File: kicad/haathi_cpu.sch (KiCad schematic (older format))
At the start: 116 parts

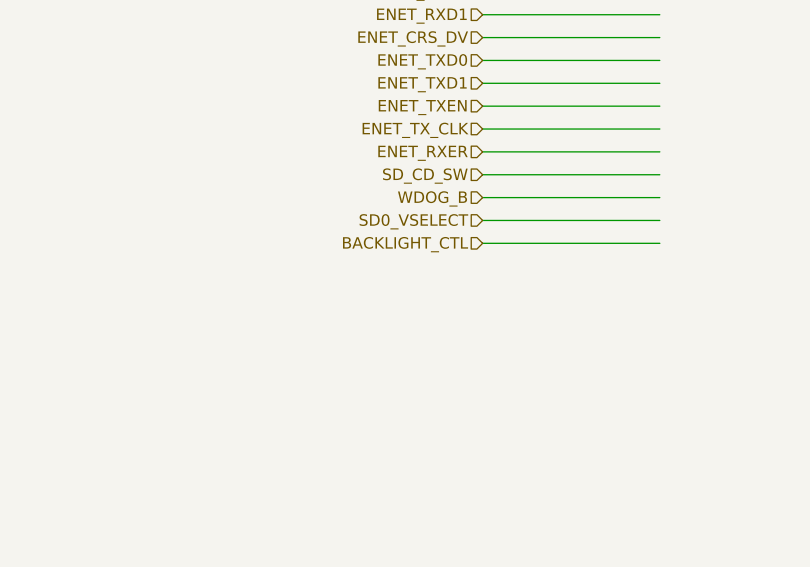
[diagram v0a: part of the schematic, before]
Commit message: Rearrange buttons and LED pin connections
LED pins go to PWM pins
Switches go to previously SPDIF_IN and OUT pins
FlexSPI 2 pins freed up

Signed-off-by: Kumar Abhishek <abhishek@theembeddedkitchen.net>
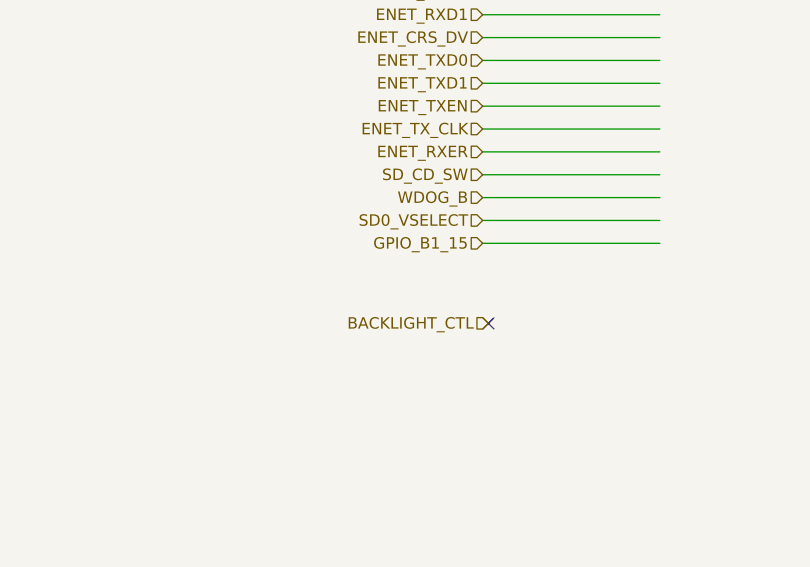
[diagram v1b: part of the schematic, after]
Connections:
- net labels added: GPIO_B1_15
- no-connect marks 2 -> 3
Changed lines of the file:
@@
 EESchema Schematic File Version 4
-LIBS:haathi_schematic-cache
+LIBS:haathi-cache
 EELAYER 26 0
 EELAYER END
 $Descr A2 23386 16535
 encoding utf-8
-Sheet 3 9
+Sheet 5 11
 Title "haathi_cam"
 Date "2018-03-11"
@@
 Text Label 3725 9000 0    50   ~ 0
 USB_OTG2_D-
-Text HLabel 10325 11050 0    50   Input ~ 0
+Text HLabel 10350 11400 0    50   Input ~ 0
 BACKLIGHT_CTL
 Wire Wire Line
@@
 Wire Wire Line
 	4100 9500 4250 9500
+Text Label 4250 9400 0    50   ~ 0
+GPIO_AD_B0_01
+Text Label 4250 9500 0    50   ~ 0
+GPIO_AD_B0_00
+Text HLabel 10325 11050 0    50   Input ~ 0
+GPIO_B1_15
+NoConn ~ 10350 11400
 Wire Bus Line
 	21850 4000 21850 4750
@@
 Wire Bus Line
 	9425 8000 9425 9800
-Text Label 4250 9400 0    50   ~ 0
-GPIO_AD_B0_01
-Text Label 4250 9500 0    50   ~ 0
-GPIO_AD_B0_00
 $EndSCHEMATC

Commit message: JTAG_MOD pullup and DNP pull down
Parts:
- added R?: 10k, symbol haathi_mayank:R
- R?: value 10k -> 10k_DNP
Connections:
- wire segments 567 -> 570
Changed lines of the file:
@@
 EESchema Schematic File Version 4
-LIBS:haathi-cache
+LIBS:haathi_cpu-cache
 EELAYER 26 0
 EELAYER END
 $Descr A2 23386 16535
 encoding utf-8
-Sheet 5 11
+Sheet 1 1
 Title "haathi_cam"
 Date "2018-03-11"
@@
 P 11850 2125
 F 0 "R?" V 11750 2075 50  0000 C CNN
-F 1 "10k" V 11966 2125 50  0000 C CNN
+F 1 "10k_DNP" V 11966 2125 50  0000 C CNN
 F 2 "" V 11780 2125 30  0000 C CNN
 F 3 "" H 11850 2125 30  0000 C CNN
@@
 GPIO_B1_15
 NoConn ~ 10350 11400
+$Comp
+L haathi_mayank:R R?
+U 1 1 5ADF8395
+P 11850 1650
+F 0 "R?" V 11750 1600 50  0000 C CNN
+F 1 "10k" V 11966 1650 50  0000 C CNN
+F 2 "" V 11780 1650 30  0000 C CNN
+F 3 "" H 11850 1650 30  0000 C CNN
+	1    11850 1650
+	1    0    0    -1
+$EndComp
+Wire Wire Line
+	11850 1800 11850 1950
+Text HLabel 11900 1300 2    50   Input ~ 0
+NVCC_GPIO_3V3
+Wire Wire Line
+	11850 1500 11850 1300
+Wire Wire Line
+	11850 1300 11900 1300
 Wire Bus Line
 	21850 4000 21850 4750

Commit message: Annotated schematic
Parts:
- gave numbers to parts that had none: 109

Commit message: ERC pass 1: Check and resolve the errors
Signed-off-by: Kumar Abhishek <abhishek@theembeddedkitchen.net>
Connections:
- net labels removed: VCC
- wire segments 570 -> 572
- no-connect marks 3 -> 5
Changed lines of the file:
@@
 EESchema Schematic File Version 4
-LIBS:haathi_schematic-cache
+LIBS:haathi-cache
 EELAYER 26 0
 EELAYER END
 $Descr A2 23386 16535
 encoding utf-8
-Sheet 3 9
+Sheet 5 11
 Title "haathi_cam"
 Date "2018-03-11"
@@
 U 1 1 5A82F303
 P 7300 3500
-F 0 "TP6" H 7453 3602 50  0000 L CNN
-F 1 "Test_Point_Probe" H 7453 3511 50  0000 L CNN
+F 0 "TP6" H 7525 3625 50  0000 C CNN
+F 1 "Test_Point_Probe" H 7775 3550 50  0000 C CNN
 F 2 "" H 7500 3500 50  0001 C CNN
 F 3 "~" H 7500 3500 50  0001 C CNN
@@
 	7050 2850 7200 2850
 Wire Wire Line
-	7200 2850 7200 4450
+	7200 2850 7200 4225
 Wire Wire Line
 	7200 4450 7200 4500
@@
 Wire Wire Line
 	7200 4800 7200 4850
-$Comp
-L power:VCC #PWR057
-U 1 1 5A8739EE
-P 7600 4450
-F 0 "#PWR057" H 7600 4300 50  0001 C CNN
-F 1 "VCC" H 7617 4623 50  0000 C CNN
-F 2 "" H 7600 4450 50  0001 C CNN
-F 3 "" H 7600 4450 50  0001 C CNN
-	1    7600 4450
-	1    0    0    -1
-$EndComp
-$Comp
-L power:PWR_FLAG #FLG010
-U 1 1 5A873B22
-P 7750 4500
-F 0 "#FLG010" H 7750 4575 50  0001 C CNN
-F 1 "PWR_FLAG" H 7750 4673 50  0000 C CNN
-F 2 "" H 7750 4500 50  0001 C CNN
-F 3 "" H 7750 4500 50  0001 C CNN
-	1    7750 4500
-	-1   0    0    1
-$EndComp
 Wire Wire Line
 	7500 4450 7600 4450
 Wire Wire Line
-	7750 4450 7750 4500
-Connection ~ 7600 4450
-Wire Wire Line
-	7600 4450 7750 4450
-Wire Wire Line
 	7050 2750 7150 2750
 Wire Wire Line
@@
 	6950 1350 6950 1650
 Wire Wire Line
-	6950 1650 7250 1650
+	6950 1650 7150 1650
 Connection ~ 6350 1350
 Wire Wire Line
@@
 	1    0    0    -1
 $EndComp
-$Comp
-L power:PWR_FLAG #FLG07
-U 1 1 5A953F34
-P 3350 4900
-F 0 "#FLG07" H 3350 4975 50  0001 C CNN
-F 1 "PWR_FLAG" H 3350 5073 50  0000 C CNN
-F 2 "" H 3350 4900 50  0001 C CNN
-F 3 "" H 3350 4900 50  0001 C CNN
-	1    3350 4900
-	-1   0    0    1
-$EndComp
 Wire Wire Line
 	6050 1350 6050 1150
@@
 	1    0    0    -1
 $EndComp
-$Comp
-L power:PWR_FLAG #FLG08
-U 1 1 5A98E537
-P 3350 5550
-F 0 "#FLG08" H 3350 5625 50  0001 C CNN
-F 1 "PWR_FLAG" H 3350 5723 50  0000 C CNN
-F 2 "" H 3350 5550 50  0001 C CNN
-F 3 "" H 3350 5550 50  0001 C CNN
-	1    3350 5550
-	-1   0    0    1
-$EndComp
 Wire Wire Line
 	1500 4900 1900 4900
@@
 	6150 11300 6250 11300
 Connection ~ 6250 11300
-Wire Wire Line
-	6250 11300 6450 11300
-$Comp
-L power:PWR_FLAG #FLG09
-U 1 1 5AEDE637
-P 6450 11300
-F 0 "#FLG09" H 6450 11375 50  0001 C CNN
-F 1 "PWR_FLAG" H 6200 11400 50  0000 C CNN
-F 2 "" H 6450 11300 50  0001 C CNN
-F 3 "" H 6450 11300 50  0001 C CNN
-	1    6450 11300
-	-1   0    0    1
-$EndComp
-Connection ~ 6450 11300
 $Comp
 L haathi_mayank:R R43
@@
 	1    0    0    -1
 $EndComp
-Connection ~ 3250 4900
-Wire Wire Line
-	3250 4900 3350 4900
 $Comp
 L power:+3V3 #PWR044
@@
 	1    0    0    -1
 $EndComp
-Connection ~ 3250 5550
-Wire Wire Line
-	3250 5550 3350 5550
 $Comp
 L power:+3V3 #PWR054
@@
 	2750 5550 3250 5550
 Wire Wire Line
-	6450 11300 6650 11300
-Wire Wire Line
 	9350 6300 9850 6300
 Text Label 9425 6300 0    50   ~ 0
@@
 	1    0    0    -1
 $EndComp
-Wire Wire Line
-	11850 1800 11850 1950
 Text HLabel 11900 1300 2    50   Input ~ 0
 NVCC_GPIO_3V3
@@
 Wire Wire Line
 	11850 1300 11900 1300
+Wire Wire Line
+	11850 1800 11850 1975
+Wire Wire Line
+	6250 11300 6650 11300
+$Comp
+L power:PWR_FLAG #FLG0103
+U 1 1 5B27BF1E
+P 7150 1525
+F 0 "#FLG0103" H 7150 1600 50  0001 C CNN
+F 1 "PWR_FLAG" H 7150 1699 50  0000 C CNN
+F 2 "" H 7150 1525 50  0001 C CNN
+F 3 "~" H 7150 1525 50  0001 C CNN
+	1    7150 1525
+	1    0    0    -1
+$EndComp
+Wire Wire Line
+	7150 1525 7150 1650
+Connection ~ 7150 1650
+Wire Wire Line
+	7150 1650 7250 1650
+$Comp
+L power:+3V3 #PWR0106
+U 1 1 5B337654
+P 7600 4450
+F 0 "#PWR0106" H 7600 4300 50  0001 C CNN
+F 1 "+3V3" H 7615 4623 50  0000 C CNN
+F 2 "" H 7600 4450 50  0001 C CNN
+F 3 "" H 7600 4450 50  0001 C CNN
+	1    7600 4450
+	1    0    0    -1
+$EndComp
+$Comp
+L power:PWR_FLAG #FLG0113
+U 1 1 5B33D17D
+P 7200 5550
+F 0 "#FLG0113" H 7200 5625 50  0001 C CNN
+F 1 "PWR_FLAG" H 7200 5724 50  0000 C CNN
+F 2 "" H 7200 5550 50  0001 C CNN
+F 3 "~" H 7200 5550 50  0001 C CNN
+	1    7200 5550
+	1    0    0    -1
+$EndComp
+$Comp
+L power:PWR_FLAG #FLG0114
+U 1 1 5B33E94E
+P 7100 4225
+F 0 "#FLG0114" H 7100 4300 50  0001 C CNN
+F 1 "PWR_FLAG" H 7450 4300 50  0000 C CNN
+F 2 "" H 7100 4225 50  0001 C CNN
+F 3 "~" H 7100 4225 50  0001 C CNN
+	1    7100 4225
+	1    0    0    -1
+$EndComp
+Wire Wire Line
+	7100 4225 7200 4225
+Connection ~ 7200 4225
+Wire Wire Line
+	7200 4225 7200 4450
+$Comp
+L power:PWR_FLAG #FLG0115
+U 1 1 5B3AC8F9
+P 8650 3050
+F 0 "#FLG0115" H 8650 3125 50  0001 C CNN
+F 1 "PWR_FLAG" H 8900 3125 50  0000 C CNN
+F 2 "" H 8650 3050 50  0001 C CNN
+F 3 "~" H 8650 3050 50  0001 C CNN
+	1    8650 3050
+	1    0    0    -1
+$EndComp
+NoConn ~ 7050 3850
+NoConn ~ 7050 3950
+$Comp
+L power:PWR_FLAG #FLG0116
+U 1 1 5B73D343
+P 8225 3450
+F 0 "#FLG0116" H 8225 3525 50  0001 C CNN
+F 1 "PWR_FLAG" H 8225 3624 50  0000 C CNN
+F 2 "" H 8225 3450 50  0001 C CNN
+F 3 "~" H 8225 3450 50  0001 C CNN
+	1    8225 3450
+	1    0    0    -1
+$EndComp
+Wire Wire Line
+	8225 3450 8225 3525
+Wire Wire Line
+	8225 3525 7300 3525
+Wire Wire Line
+	7300 3525 7300 3500
 Wire Bus Line
 	21850 4000 21850 4750
@@
 Wire Bus Line
 	9425 8000 9425 9800
+Connection ~ 7300 3500
 $EndSCHEMATC

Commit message: GPIO namings as per the datasheet except for JTAG, LCD and SDRAM. Pull up/downs in the respective peripheral sheet.
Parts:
- removed C97: 0.1uF, symbol haathi_mayank:C_NP
- removed R53, R55: 4.7k_DNP, symbol haathi_mayank:R
- removed R54, R56: 4.7k, symbol haathi_mayank:R
- removed R57, R58: 10k, symbol haathi_mayank:R
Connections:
- net labels added: GPIO_AD_B0_12, GPIO_AD_B0_13, GPIO_AD_B0_14, GPIO_AD_B0_15, GPIO_B1_04, GPIO_B1_05, GPIO_B1_06, GPIO_B1_07, GPIO_B1_08, GPIO_B1_09, GPIO_B1_10, GPIO_B1_11, GPIO_B1_12, GPIO_B1_13, GPIO_B1_14, GPIO_EMC_39, GPIO_EMC_40, GPIO_EMC_41, GPIO_SD_B0_01, GPIO_SD_B0_04, GPIO_SD_B0_05, GPIO_SD_B1_00, GPIO_SD_B1_03, GPIO_SD_B1_06, GPIO_SD_B1_07, GPIO_SD_B1_08, GPIO_SD_B1_09, GPIO_SD_B1_10, GPIO_SD_B1_11
- net labels removed: AUD_INT, BACKLIGHT_CTL, CAN2_RX, CAN2_TX, ENET_CRS_DV, ENET_MDC, ENET_MDIO, ENET_RXD0, ENET_RXD1, ENET_RXER, ENET_TXD0, ENET_TXD1, ENET_TXEN, ENET_TX_CLK, FlexSPI_CLK, FlexSPI_CLK_B, FlexSPI_D0_A, FlexSPI_D0_B, FlexSPI_D1_A, FlexSPI_D1_B, FlexSPI_D2_A, FlexSPI_D2_B, FlexSPI_D3_A, FlexSPI_D3_B, FlexSPI_SS0, FlexSPI_SS_B, I2C1_SCL, I2C1_SDA, I2C2_SCL, I2C2_SDA, SAI1_MCLK, SAI1_RXD, SAI1_RX_BCLK, SAI1_RX_SYNC, SAI1_TXD, SAI1_TX_BCLK, SAI1_TX_SYNC, SD0_VSELECT, SD1_CLK, SD1_CMD, SD1_D0, SD1_D1, SD1_D2, SD1_D3, SD_CD_SW, SD_PWREN, SEMC_DQS, UART1_RXD, UART1_TXD, WDOG_B
- wire segments 572 -> 548
- no-connect marks 5 -> 4

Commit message: Clean up of USB OTG labels
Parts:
- removed R34, R35: 0E_DNP, symbol haathi_mayank:R
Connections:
- net labels removed: USB_OTG1_ID, USB_OTG2_ID
- wire segments 548 -> 544
- no-connect marks 4 -> 2
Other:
- note removed: "USB_OTG\n"
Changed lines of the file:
@@
 EESchema Schematic File Version 4
-LIBS:haathi_schematic-cache
+LIBS:haathi_cpu-cache
 EELAYER 26 0
 EELAYER END
 $Descr A2 23386 16535
 encoding utf-8
-Sheet 1 9
+Sheet 1 1
 Title "haathi_cam"
 Date "2018-03-11"
@@
 Text Label 17450 9850 0    50   ~ 0
 GPIO_SD_B1_05
-Text Notes 6050 9450 2    98   ~ 0
-USB_OTG\n
 Wire Wire Line
 	4250 8500 3650 8500
@@
 Text Label 7200 14750 0    50   ~ 0
 GPIO_AD_B0_05
-Text HLabel 3650 9400 0    50   Input ~ 0
-USB_OTG1_ID
-Text HLabel 3650 9500 0    50   Input ~ 0
-USB_OTG2_ID
-$Comp
-L haathi_mayank:R R34
-U 1 1 5AE1CD1D
-P 3950 9400
-F 0 "R34" V 4157 9400 50  0000 C CNN
-F 1 "0E_DNP" V 4066 9400 50  0000 C CNN
-F 2 "" V 3880 9400 30  0000 C CNN
-F 3 "" H 3950 9400 30  0000 C CNN
-	1    3950 9400
-	0    -1   -1   0
-$EndComp
-$Comp
-L haathi_mayank:R R35
-U 1 1 5AE1DA1A
-P 3950 9500
-F 0 "R35" V 4157 9500 50  0000 C CNN
-F 1 "0E_DNP" V 4066 9500 50  0000 C CNN
-F 2 "" V 3880 9500 30  0000 C CNN
-F 3 "" H 3950 9500 30  0000 C CNN
-	1    3950 9500
-	0    -1   1    0
-$EndComp
-Wire Wire Line
-	3650 9400 3800 9400
-Wire Wire Line
-	3650 9500 3800 9500
-Wire Wire Line
-	4100 9400 4250 9400
-Wire Wire Line
-	4100 9500 4250 9500
-Text Label 4250 9400 0    50   ~ 0
-GPIO_AD_B0_01
-Text Label 4250 9500 0    50   ~ 0
-GPIO_AD_B0_00
 Text HLabel 10325 11050 0    50   Input ~ 0
 GPIO_B1_15
@@
 	1    0    0    -1
 $EndComp
-NoConn ~ 7050 3850
-NoConn ~ 7050 3950
 $Comp
 L power:PWR_FLAG #FLG0116
